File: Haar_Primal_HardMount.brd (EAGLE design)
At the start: 24.9 x 11 mm, 10 parts, among them J1 SOLDERCUP_CONN_QUAD, Q1 DMG3404, U1 SHT30DFN, U4 DPS368

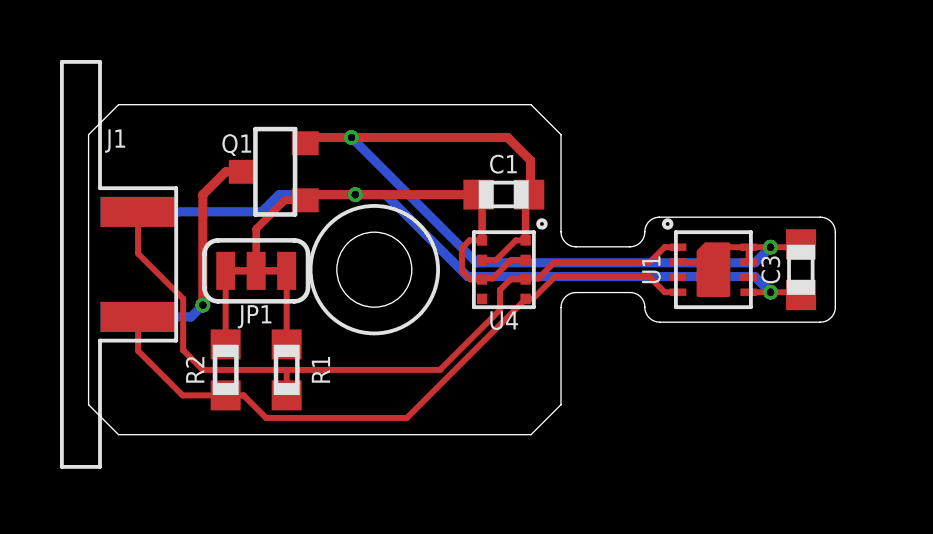
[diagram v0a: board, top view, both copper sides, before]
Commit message: Updated Hard Mount - Variable address jumper
Added jumper to Hard Mount to allow for a variable address configuration
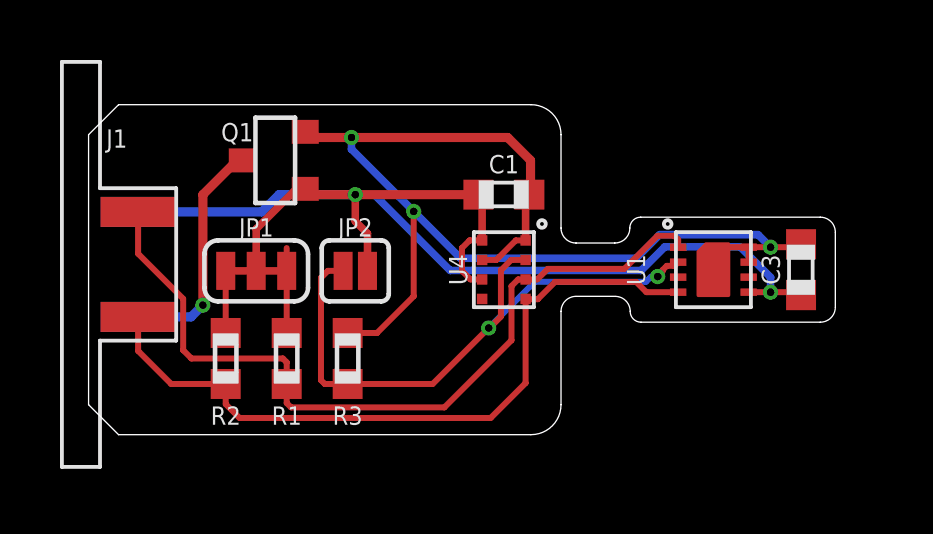
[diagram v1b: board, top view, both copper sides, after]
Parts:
- removed H2: (no value), bschulz:2_56
- added JP2: JUMPER-SMT_2_NO_SILK, bschulz:SMT-JUMPER_2_NO_SILK
- added R3: 10k, bschulz_passives:R0603
- moved Q1 0.38 mm to (6.22, 9.14)
- moved R1 0.38 mm to (6.60, 2.54)
- moved R2 0.38 mm to (4.57, 2.54)
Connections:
- new net ADDR: JP2.1, R3.2, U1.2, U4.2
- net 3V3: now also JP2.2; no longer U4.2
- net GND: now also R3.1; no longer U1.2
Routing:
- net ADDR: track 0.00 -> 21.0 mm, vias 0 -> 2
- net GND: track 33.5 -> 38.5 mm, vias 2 -> 3
- net SDA: track 25.2 -> 27.4 mm
- net 3V3: track 39.1 -> 41.2 mm
- net SCL: track 22.2 -> 24.1 mm
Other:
- outline, holes or cut-outs redrawn

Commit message: Hard Mount v1.1 Update
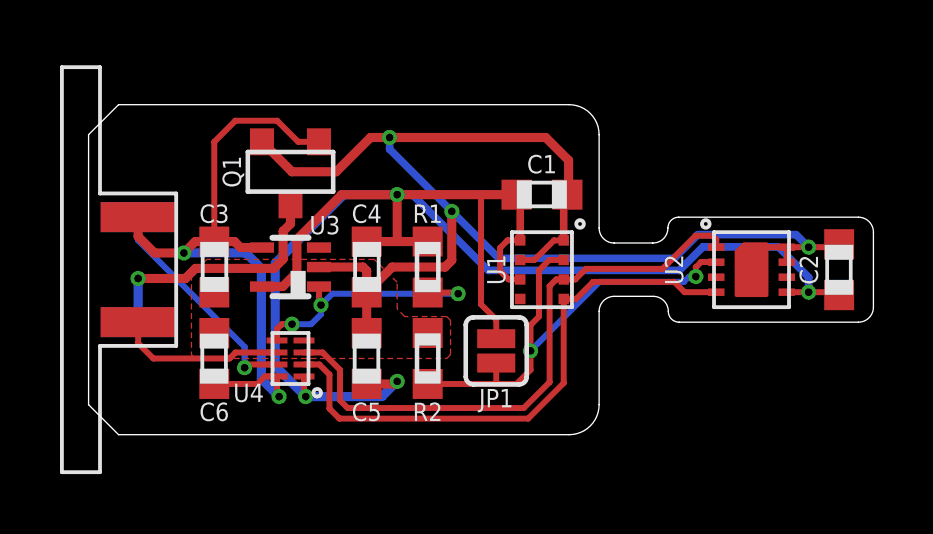
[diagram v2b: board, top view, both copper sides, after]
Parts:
- removed JP2: JUMPER-SMT_2_NO_SILK, bschulz:SMT-JUMPER_2_NO_SILK
- removed R3: 10k, bschulz_passives:R0603
- added C2, C5, C6: 0.1uF, bschulz_passives:C0603
- added C4: 1uF, bschulz_passives:C0603
- added U2: SHT31DFN, bschulz:DFN_8_2.5X2.5
- added U3: TPS79733, bschulz:DCK_R-PDSO-G5
- C3: value 0.1uF -> 1uF
- J1: value SOLDERCUP_CONN_QUAD -> CONN_I2C_SENSOR_EDGE_MOUNT; device bschulz:SOLDERCUP_CONN_QUAD -> GEMS_Plugs:SOLDERCUP_CONN_QUAD
- JP1: value JUMPER-SMT_3_2-NC_TRACE_SILK -> JUMPER-SMT_2_NO_SILK; device bschulz:SMT-JUMPER_3_2-NC_TRACE_SILK -> bschulz:SMT-JUMPER_2_NO_SILK
- U1: value SHT30DFN -> DPS368; device bschulz:DFN_8_2.5X2.5 -> bschulz:PG-VLGA-8
- U4: value DPS368 -> TXS0102DQM; device bschulz:PG-VLGA-8 -> bschulz:DQM_R-PX2SON-N8
- moved C3 19.6 mm to (4.19, 5.59), turned to 270 degrees
- moved JP1 8.43 mm to (13.6, 2.79), turned to 90 degrees
- moved U4 7.70 mm to (6.73, 2.54), turned to 90 degrees
- moved R2 6.73 mm to (11.3, 2.54), turned to 270 degrees
- moved U1 5.71 mm to (15.1, 5.50)
- moved R1 5.60 mm to (11.3, 5.59)
- moved C1 1.27 mm to (15.1, 8.00)
- moved Q1 0.64 mm to (6.73, 8.76), turned to 180 degrees
- moved J1 0.18 mm to (0.38, 5.50)
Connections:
- removed net N$1: JP1.3, R1.2
- removed net N$2: JP1.1, R2.2
- new net PG: R1.1, U3.1, U4.5
- new net SCL_HV: J1.3, U4.7
- new net SDA_HV: J1.1, U4.6
- new net VIN+: C3.1, C6.1, J1.2, Q1.1, U3.4, U4.8
- net 3V3: now also C2.1, C4.1, C5.1, R1.2, U1.6, U1.8, U2.5, U3.5, U4.1; no longer C3.1, J1.3, JP2.2, Q1.1, U1.5, U4.6, U4.8
- net ADDR: now also JP1.1, R2.2, U2.2; no longer JP2.1, R3.2, U4.2
- net GND: now also C2.2, C4.2, C5.2, C6.2, R2.1, U1.1, U2.7, U2.8, U2.EP, U3.2, U4.4; no longer R3.1, U1.8, U1.EP, U4.1, U4.7
- net INT_PRES: now also U1.5; no longer U4.5
- net INT_RH: now also U2.3; no longer U1.3
- net SCL: now also U2.4, U4.2; no longer J1.1, R2.1, U4.4
- net SDA: now also U1.3, U2.1; no longer J1.2, R1.1, U1.1
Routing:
- net VIN+: track 0.00 -> 22.8 mm, vias 0 -> 2
- net 3V3: track 41.2 -> 55.6 mm, vias 2 -> 4
- net PG: track 0.00 -> 8.76 mm, vias 0 -> 3
- net SDA: track 27.4 -> 19.7 mm
- net SCL_HV: track 0.00 -> 7.61 mm, vias 0 -> 1
- net GND: track 38.5 -> 45.0 mm
- net SDA_HV: track 0.00 -> 5.63 mm
- net SCL: track 24.1 -> 18.8 mm
- net ADDR: track 21.0 -> 16.3 mm
- net N$1: track 2.83 -> 0.00 mm
- net N$2: track 1.94 -> 0.00 mm
- net VIN-: track 7.79 -> 8.47 mm
- added copper zone on layer 1, net GND
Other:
- board size 24.9 x 11 mm -> 26.2 x 11 mm
- board text added: "Project Haar - Primal Hard Mount v1.1 Bobby Schulz - UMN/GEMS"
- board text added: "SHT3"
- board text added: "V+"
- board text added: "V-"
- board text added: "Vcc: 3V ~ 5V Logic: Vcc"
- board text removed: "3v3"
- board text removed: "GND"
- board text removed: "Project Haar - Primal Hard Mount v0.1 Bobby Schulz - UMN/GEMS"

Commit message: v2.0 Updates - Generated Gerbers
Fixed ADDR pinout to DPS368
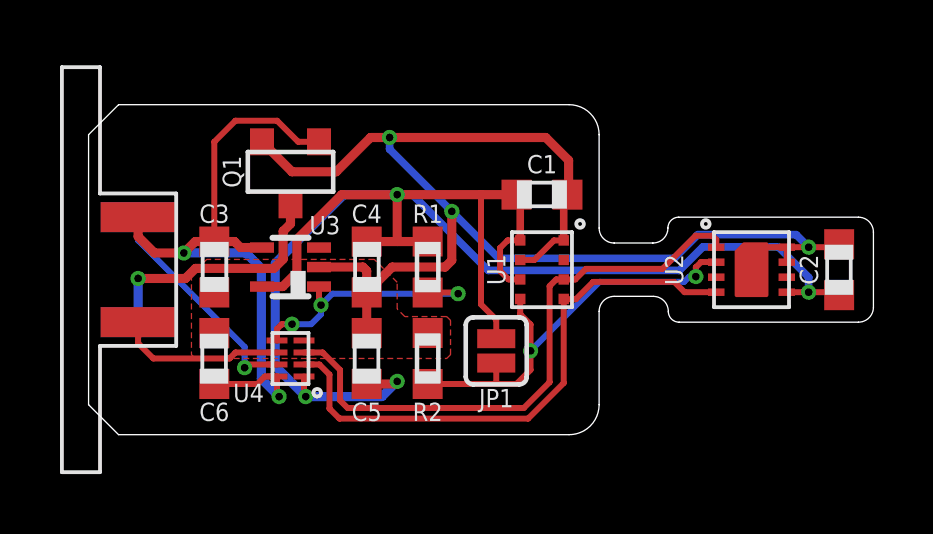
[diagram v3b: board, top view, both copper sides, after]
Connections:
- removed net INT_PRES: U1.5
- net ADDR: now also U1.5; no longer U1.2
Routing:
- net ADDR: track 16.3 -> 14.4 mm
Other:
- board text added: "Project Haar - Primal Hard Mount v2.0 Bobby Schulz - UMN/GEMS"
- board text removed: "Project Haar - Primal Hard Mount v1.1 Bobby Schulz - UMN/GEMS"
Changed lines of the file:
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@@
 <grid distance="50" unitdist="mil" unit="mm" style="lines" multiple="1" display="no" altdistance="5" altunitdist="mil" altunit="mm"/>
 <layers>
-<layer number="1" name="Top" color="4" fill="1" visible="no" active="yes"/>
+<layer number="1" name="Top" color="4" fill="1" visible="yes" active="yes"/>
 <layer number="2" name="Route2" color="16" fill="1" visible="no" active="no"/>
 <layer number="3" name="Route3" color="17" fill="1" visible="no" active="no"/>
@@
 <layer number="19" name="Unrouted" color="6" fill="1" visible="yes" active="yes"/>
 <layer number="20" name="Dimension" color="24" fill="1" visible="yes" active="yes"/>
-<layer number="21" name="tPlace" color="7" fill="1" visible="no" active="yes"/>
+<layer number="21" name="tPlace" color="7" fill="1" visible="yes" active="yes"/>
 <layer number="22" name="bPlace" color="7" fill="1" visible="yes" active="yes"/>
-<layer number="23" name="tOrigins" color="15" fill="1" visible="no" active="yes"/>
+<layer number="23" name="tOrigins" color="15" fill="1" visible="yes" active="yes"/>
 <layer number="24" name="bOrigins" color="15" fill="1" visible="yes" active="yes"/>
-<layer number="25" name="tNames" color="7" fill="1" visible="no" active="yes"/>
+<layer number="25" name="tNames" color="7" fill="1" visible="yes" active="yes"/>
 <layer number="26" name="bNames" color="7" fill="1" visible="yes" active="yes"/>
 <layer number="27" name="tValues" color="7" fill="1" visible="no" active="yes"/>
@@
 <layer number="37" name="tTest" color="7" fill="1" visible="no" active="yes"/>
 <layer number="38" name="bTest" color="7" fill="1" visible="no" active="yes"/>
-<layer number="39" name="tKeepout" color="4" fill="11" visible="no" active="yes"/>
+<layer number="39" name="tKeepout" color="4" fill="11" visible="yes" active="yes"/>
 <layer number="40" name="bKeepout" color="1" fill="11" visible="yes" active="yes"/>
-<layer number="41" name="tRestrict" color="4" fill="10" visible="no" active="yes"/>
+<layer number="41" name="tRestrict" color="4" fill="10" visible="yes" active="yes"/>
 <layer number="42" name="bRestrict" color="1" fill="10" visible="yes" active="yes"/>
 <layer number="43" name="vRestrict" color="2" fill="10" visible="no" active="yes"/>
@@
 <layer number="49" name="Reference" color="7" fill="1" visible="no" active="yes"/>
 <layer number="50" name="dxf" color="7" fill="1" visible="no" active="no"/>
-<layer number="51" name="tDocu" color="7" fill="1" visible="no" active="yes"/>
+<layer number="51" name="tDocu" color="7" fill="1" visible="yes" active="yes"/>
 <layer number="52" name="bDocu" color="7" fill="1" visible="yes" active="yes"/>
 <layer number="53" name="tGND_GNDA" color="7" fill="1" visible="no" active="no"/>
@@
 <text x="16.764" y="2.794" size="0.6096" layer="52" font="vector" ratio="15" rot="MR0" align="center-left">Project Haar - Primal
 Hard Mount
-v1.1
+v2.0
 Bobby Schulz - UMN/GEMS</text>
 <wire x1="25.662" y1="3.75" x2="26.162" y2="4.25" width="0" layer="20" curve="90"/>
@@
 <wire x1="1.651" y1="5.207" x2="1.651" y2="3.75" width="0.3048" layer="16"/>
 </signal>
-<signal name="INT_PRES">
-<contactref element="U1" pad="5"/>
-</signal>
 <signal name="INT_RH">
 <contactref element="U2" pad="3"/>
@@
 <signal name="ADDR">
 <contactref element="U2" pad="2"/>
-<contactref element="U1" pad="2"/>
 <via x="20.2416" y="5.27109375" extent="1-16" drill="0.254"/>
 <wire x1="20.923" y1="5.75" x2="20.9186" y2="5.7544" width="0.2" layer="1"/>
@@
 <wire x1="17.0332" y1="5.0952" x2="14.732" y2="2.794" width="0.2" layer="16"/>
 <via x="14.732" y="2.794" extent="1-16" drill="0.254"/>
-<wire x1="14.732" y1="2.794" x2="14.732" y2="3.6544" width="0.2" layer="1"/>
-<wire x1="15.0146" y1="3.937" x2="14.732" y2="3.6544" width="0.2" layer="1"/>
-<wire x1="15.0146" y1="3.937" x2="15.0146" y2="5.479975" width="0.2" layer="1"/>
-<wire x1="15.359625" y1="5.825" x2="15.838" y2="5.825" width="0.2" layer="1"/>
 <wire x1="19.84791875" y1="5.0952" x2="17.0332" y2="5.0952" width="0.2" layer="16"/>
-<wire x1="15.0146" y1="5.479975" x2="15.359625" y2="5.825" width="0.2" layer="1"/>
 <wire x1="11.303" y1="1.69" x2="13.589" y2="1.69" width="0.2" layer="1"/>
 <wire x1="13.589" y1="1.69" x2="14.263" y2="1.69" width="0.2" layer="1"/>
@@
 <wire x1="14.732" y1="2.159" x2="14.732" y2="2.794" width="0.2" layer="1"/>
 <wire x1="13.589" y1="2.3876" x2="13.589" y2="1.69" width="0.2" layer="1"/>
+<contactref element="U1" pad="5"/>
+<wire x1="14.732" y1="3.673" x2="14.388" y2="4.017" width="0.2" layer="1"/>
+<wire x1="14.388" y1="4.017" x2="14.388" y2="4.525" width="0.2" layer="1"/>
+<wire x1="14.732" y1="2.794" x2="14.732" y2="3.673" width="0.2" layer="1"/>
 </signal>
 <signal name="PG">
